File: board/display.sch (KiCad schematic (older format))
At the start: 12 parts, among them U201 MAN74A, U202 MAN74A, U203 MAN74A, U204 MAN74A, U205 MAN74A, U206 MAN74A, U207 MAN74A, U208 MAN74A, U209 MAX7219

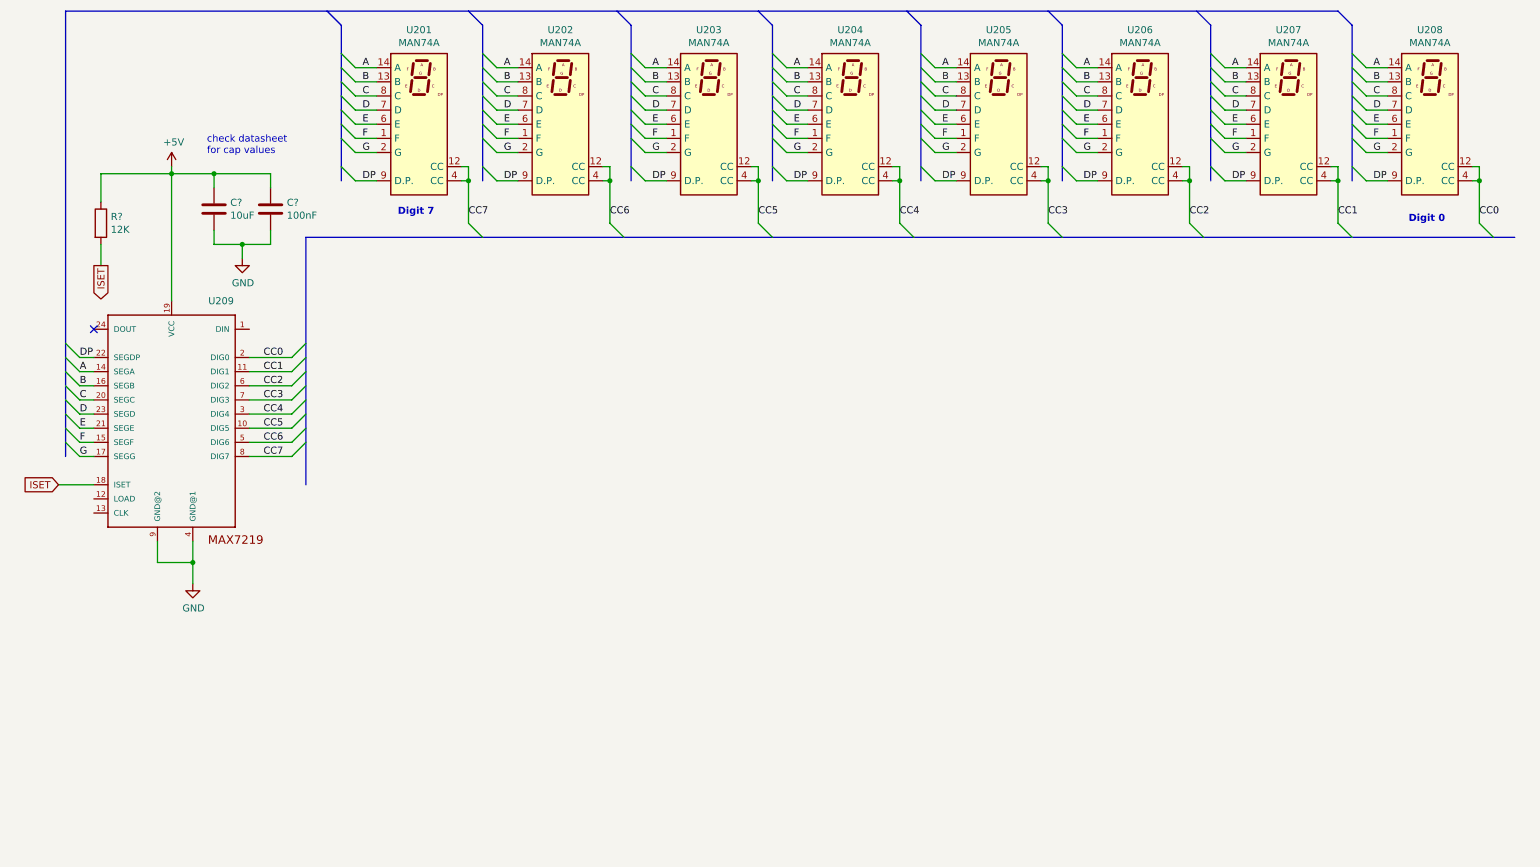
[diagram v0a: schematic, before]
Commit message: update schematic with switches, fix up default config
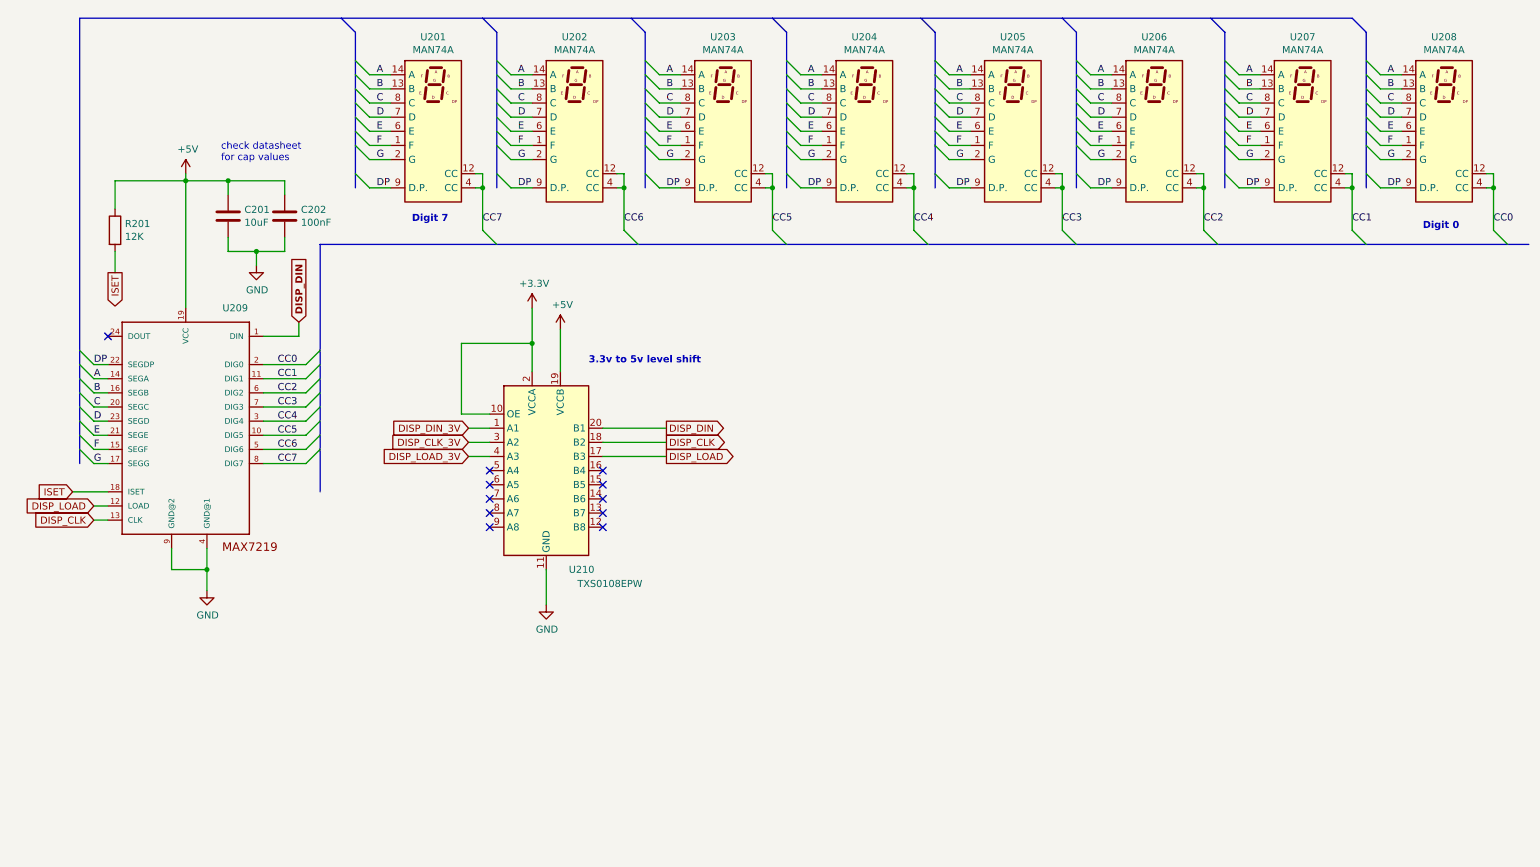
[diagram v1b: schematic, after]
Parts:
- added U210: TXS0108EPW, Package_SO:TSSOP-20_4.4x6.5mm_P0.65mm, symbol Logic_LevelTranslator:TXS0108EPW
- gave numbers to parts that had none: 3
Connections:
- net +5V: now also U210.19 (VCCB)
- net GND: now also U210.11 (GND)
- net DISP_DIN: now reaches U209.1 (DIN)
- net DISP_DIN: now also U210.20 (B1)
- net DISP_LOAD: now reaches U209.12 (LOAD)
- net DISP_LOAD: now also U210.17 (B3)
- net DISP_CLK: now reaches U209.13 (CLK)
- net DISP_CLK: now also U210.18 (B2)
- new net +3V3: U210.10 (OE), U210.2 (VCCA)
- new net DISP_CLK_3V: U210.3 (A2)
- new net DISP_DIN_3V: U210.1 (A1)
- new net DISP_LOAD_3V: U210.4 (A3)
- no-connect marks 1 -> 11
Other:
- note added: "3.3v to 5v level shift"
- moved on the sheet: C201, C202, R201, U201, U202, U203, U204, U205, U206, U207, U208, U209

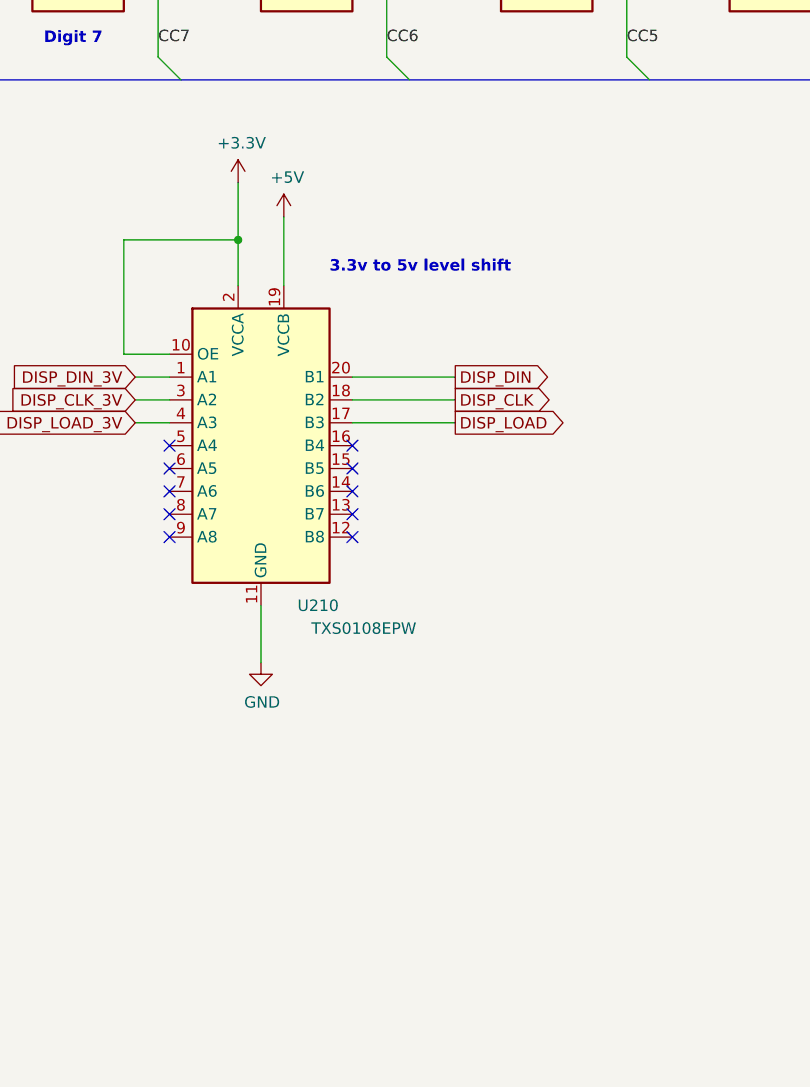
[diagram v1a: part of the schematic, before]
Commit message: Switch board over to using a0 for clapper input and add voltage divider. This frees up a pin for timecode output.
always increment the clock regardless of internal setting (clock
generation tbd)
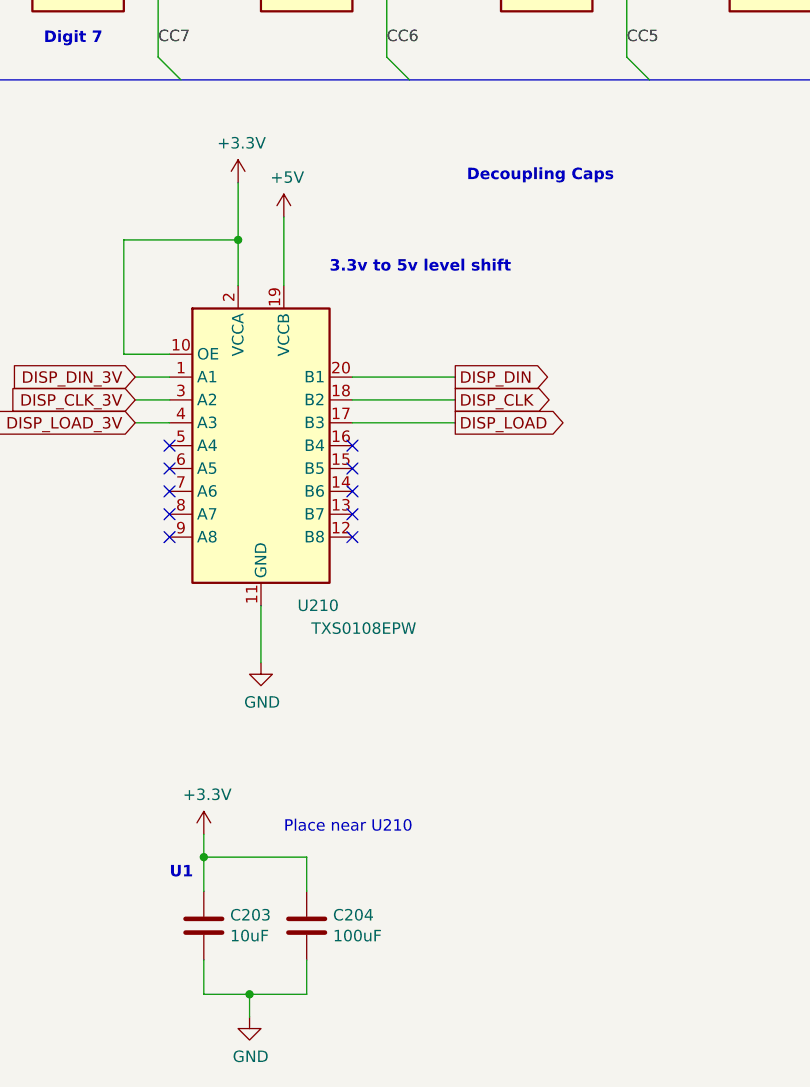
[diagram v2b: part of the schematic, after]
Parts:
- added C203: 10uF, symbol Device:C
- added C204: 100uF, symbol Device:C
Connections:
- net +3V3: now also C203.1, C204.1
- net GND: now also C203.2, C204.2
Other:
- note added: "Decoupling Caps\n"
- note added: "Place near U210"
- note added: "U1\n"
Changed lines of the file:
@@
 Text Notes 4500 3650 0    50   ~ 10
 3.3v to 5v level shift
+$Comp
+L Device:C C?
+U 1 1 5FA69937
+P 3950 6500
+AR Path="/5FA69937" Ref="C?"  Part="1"
+AR Path="/5F5A5FDC/5FA69937" Ref="C203"  Part="1"
+F 0 "C203" H 4065 6546 50  0000 L CNN
+F 1 "10uF" H 4065 6455 50  0000 L CNN
+F 2 "" H 3988 6350 50  0001 C CNN
+F 3 "~" H 3950 6500 50  0001 C CNN
+	1    3950 6500
+	1    0    0    -1
+$EndComp
+$Comp
+L Device:C C?
+U 1 1 5FA6993D
+P 4400 6500
+AR Path="/5FA6993D" Ref="C?"  Part="1"
+AR Path="/5F5A5FDC/5FA6993D" Ref="C204"  Part="1"
+F 0 "C204" H 4515 6546 50  0000 L CNN
+F 1 "100uF" H 4515 6455 50  0000 L CNN
+F 2 "" H 4438 6350 50  0001 C CNN
+F 3 "~" H 4400 6500 50  0001 C CNN
+	1    4400 6500
+	1    0    0    -1
+$EndComp
+Wire Wire Line
+	3950 6650 3950 6800
+Wire Wire Line
+	3950 6800 4150 6800
+Wire Wire Line
+	4400 6800 4400 6650
+$Comp
+L power:GND #PWR?
+U 1 1 5FA69946
+P 4150 6900
+AR Path="/5FA69946" Ref="#PWR?"  Part="1"
+AR Path="/5F5A5FDC/5FA69946" Ref="#PWR0208"  Part="1"
+F 0 "#PWR0208" H 4150 6650 50  0001 C CNN
+F 1 "GND" H 4155 6727 50  0000 C CNN
+F 2 "" H 4150 6900 50  0001 C CNN
+F 3 "" H 4150 6900 50  0001 C CNN
+	1    4150 6900
+	1    0    0    -1
+$EndComp
+Wire Wire Line
+	4150 6900 4150 6800
+Connection ~ 4150 6800
+Wire Wire Line
+	4150 6800 4400 6800
+Text Notes 5100 3250 0    50   ~ 10
+Decoupling Caps\n
+$Comp
+L power:+3.3V #PWR?
+U 1 1 5FA69950
+P 3950 6100
+AR Path="/5FA69950" Ref="#PWR?"  Part="1"
+AR Path="/5F5A5FDC/5FA69950" Ref="#PWR0207"  Part="1"
+F 0 "#PWR0207" H 3950 5950 50  0001 C CNN
+F 1 "+3.3V" H 3965 6273 50  0000 C CNN
+F 2 "" H 3950 6100 50  0001 C CNN
+F 3 "" H 3950 6100 50  0001 C CNN
+	1    3950 6100
+	1    0    0    -1
+$EndComp
+Wire Wire Line
+	3950 6100 3950 6200
+Wire Wire Line
+	3950 6200 4400 6200
+Wire Wire Line
+	4400 6200 4400 6350
+Connection ~ 3950 6200
+Wire Wire Line
+	3950 6200 3950 6350
+Text Notes 3800 6300 0    50   ~ 10
+U1\n
+Text Notes 4300 6100 0    50   ~ 0
+Place near U210
 Wire Bus Line
 	900  1200 900  4350
